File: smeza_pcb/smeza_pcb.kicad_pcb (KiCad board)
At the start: 2 copper layers, 76.2 x 76.2 mm, 59 parts, among them J1 SS-90000-002, J2 SS-90000-002, J3 Conn_01x03, J4 Conn_01x04, J5 Conn_01x03, J6 Conn_01x03, J7 Conn_01x03, J8 Conn_01x03, J9 Conn_02x03_Odd_Even, SW1 SW_DIP_x04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

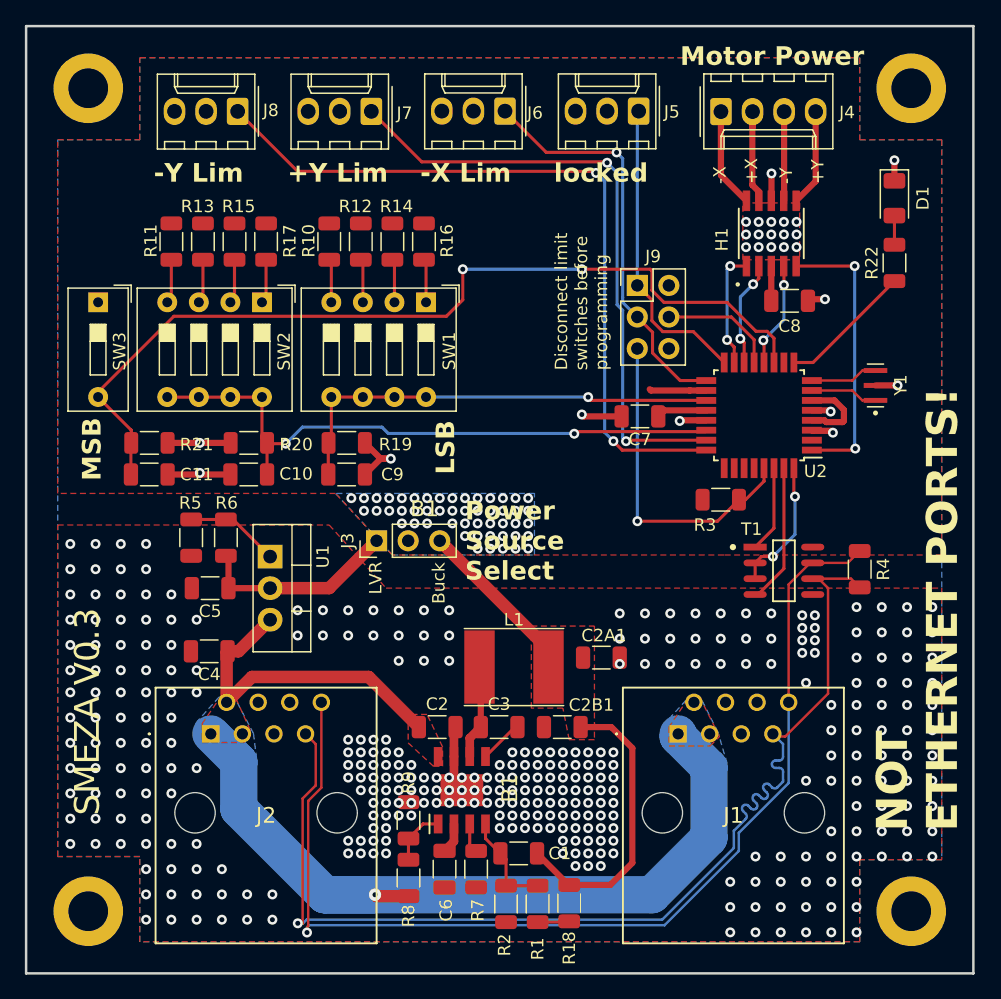
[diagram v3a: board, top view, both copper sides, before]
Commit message: Replaced most extended parts. Swapped out many 1206 resistors for 0805 resistors. Swapped out C1. Swapped out LED. Made all headers DNP. Rerouted to reflect the new footprints.
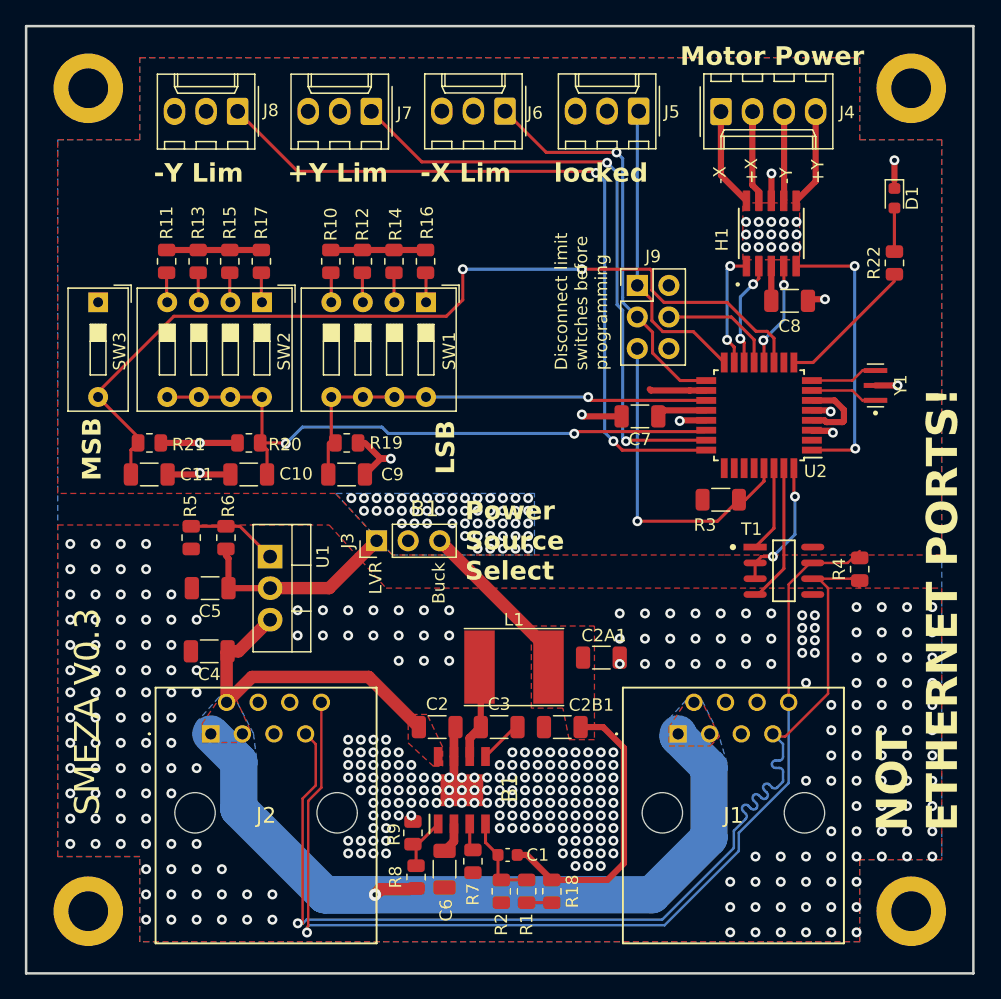
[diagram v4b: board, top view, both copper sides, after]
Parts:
- C1: footprint Capacitor_SMD:C_1206_3216Metric -> Capacitor_SMD:C_0603_1608Metric
- D1: footprint LED_SMD:LED_1206_3216Metric -> LED_SMD:LED_0603_1608Metric
- R1, R10, R11, R12, R13, R14, R15, R16, R17, R18, R19, R2, R20, R21, R22, R4, R5, R6, R7, R8, R9: footprint Resistor_SMD:R_1206_3216Metric -> Resistor_SMD:R_0805_2012Metric
- moved R18 1.69 mm to (143.9, 122.9)
- moved R11 1.63 mm to (112.9, 72.3)
- moved R13 1.63 mm to (115.4, 72.3)
- moved R15 1.63 mm to (118.0, 72.3)
- moved R17 1.63 mm to (120.5, 72.3)
- moved R10 1.59 mm to (126.1, 72.3)
- moved R12 1.59 mm to (128.7, 72.3)
- moved R14 1.59 mm to (131.2, 72.3)
- moved R16 1.59 mm to (133.7, 72.3)
- moved R1 1.35 mm to (141.9, 122.9)
- moved R2 1.09 mm to (139.8, 122.9)
- moved R9 1.07 mm to (132.7, 118.2)
- moved C1 0.90 mm to (140.3, 120.0)
- moved R7 0.69 mm to (137.5, 120.5)
- moved R8 0.61 mm to (133.0, 121.8)
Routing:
- net /+5V: track 13.8 -> 29.1 mm
- net Net-(D1-A): track 2.34 -> 3.50 mm
- net Net-(R15-Pad2): track 3.56 -> 2.40 mm
- net Net-(R13-Pad2): track 3.56 -> 2.40 mm
- net Net-(R11-Pad2): track 3.56 -> 2.40 mm
- net Net-(R17-Pad2): track 3.56 -> 2.40 mm
- net Net-(B1-FB): track 8.19 -> 7.06 mm
- net Net-(R14-Pad2): track 3.49 -> 2.40 mm
- net Net-(R12-Pad2): track 3.49 -> 2.40 mm
- net Net-(R10-Pad2): track 3.49 -> 2.40 mm
- net Net-(R16-Pad2): track 3.49 -> 2.40 mm
- net /DIPS58: track 50.3 -> 50.9 mm
- net /TransceiverDriverEnable: track 11.4 -> 10.8 mm
- net Net-(R1-Pad1): track 2.57 -> 2.03 mm

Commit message: Added tooling holes
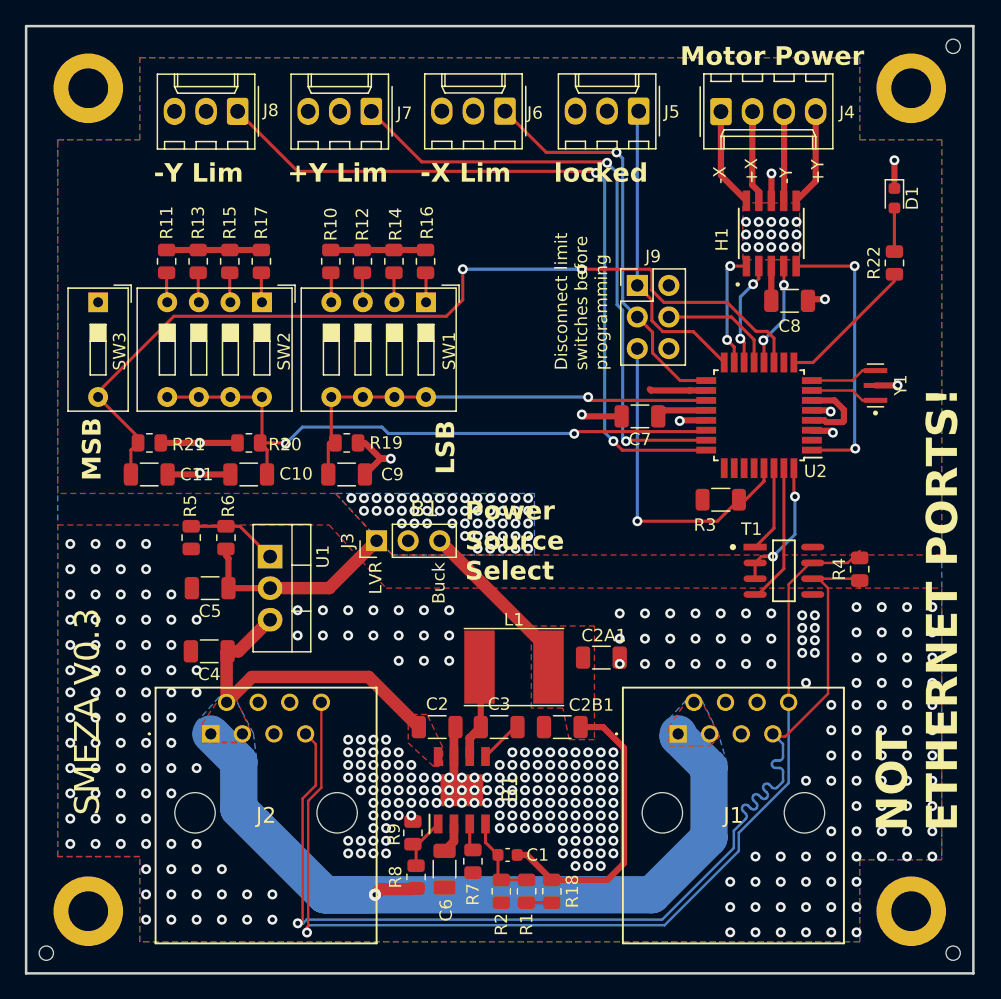
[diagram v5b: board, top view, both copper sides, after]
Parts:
- added FAB**: ToolingHole, Footprints:ToolingHole, F.Cu at (176.2, 55.0)
- added FAB**: ToolingHole, Footprints:ToolingHole, F.Cu at (103.2, 127.9)
- added FAB**: ToolingHole, Footprints:ToolingHole, F.Cu at (176.2, 127.9)
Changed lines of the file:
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@@
     )
+  )
+  (footprint "Footprints:ToolingHole" (layer "F.Cu")
+    (at 176.1744 54.9656)
+    (attr through_hole board_only)
+    (fp_text reference "FAB**" (at 0 -0.5 unlocked) (layer "F.Fab")
+        (effects (font (size 1 1) (thickness 0.1)))
+    )
+    (fp_text value "ToolingHole" (at 0 1 unlocked) (layer "F.Fab")
+        (effects (font (size 1 1) (thickness 0.15)))
+    )
+    (fp_text user "${REFERENCE}" (at 0 2.5 unlocked) (layer "F.Fab")
+        (effects (font (size 1 1) (thickness 0.15)))
+    )
+    (fp_circle (center 0 0) (end 1.016 0)
+      (stroke (width 0.05) (type solid)) (fill none) (layer "B.CrtYd"))
+    (fp_circle (center 0 0) (end 1.016 0)
+      (stroke (width 0.05) (type solid)) (fill none) (layer "F.CrtYd"))
+    (pad "" np_thru_hole circle (at 0 0) (size 1.152 1.152) (drill 1.152) (layers "F&B.Cu" "*.Mask")
+      (solder_mask_margin 0.148))
   )
   (footprint "Resistor_SMD:R_0805_2012Metric" (layer "F.Cu")
@@
     (pad "1" thru_hole circle locked (at 0 0) (size 5.6 5.6) (drill 3.2) (layers "*.Cu" "*.Mask"))
   )
+  (footprint "Footprints:ToolingHole" (layer "F.Cu")
+    (at 103.2256 127.9144)
+    (attr through_hole board_only)
+    (fp_text reference "FAB**" (at 0 -0.5 unlocked) (layer "F.Fab")
+        (effects (font (size 1 1) (thickness 0.1)))
+    )
+    (fp_text value "ToolingHole" (at 0 1 unlocked) (layer "F.Fab")
+        (effects (font (size 1 1) (thickness 0.15)))
+    )
+    (fp_text user "${REFERENCE}" (at 0 2.5 unlocked) (layer "F.Fab")
+        (effects (font (size 1 1) (thickness 0.15)))
+    )
+    (fp_circle (center 0 0) (end 1.016 0)
+      (stroke (width 0.05) (type solid)) (fill none) (layer "B.CrtYd"))
+    (fp_circle (center 0 0) (end 1.016 0)
+      (stroke (width 0.05) (type solid)) (fill none) (layer "F.CrtYd"))
+    (pad "" np_thru_hole circle (at 0 0) (size 1.152 1.152) (drill 1.152) (layers "F&B.Cu" "*.Mask")
+      (solder_mask_margin 0.148))
+  )
+  (footprint "Footprints:ToolingHole" (layer "F.Cu")
+    (at 176.1744 127.9144)
+    (attr through_hole board_only)
+    (fp_text reference "FAB**" (at 0 -0.5 unlocked) (layer "F.Fab")
+        (effects (font (size 1 1) (thickness 0.1)))
+    )
+    (fp_text value "ToolingHole" (at 0 1 unlocked) (layer "F.Fab")
+        (effects (font (size 1 1) (thickness 0.15)))
+    )
+    (fp_text user "${REFERENCE}" (at 0 2.5 unlocked) (layer "F.Fab")
+        (effects (font (size 1 1) (thickness 0.15)))
+    )
+    (fp_circle (center 0 0) (end 1.016 0)
+      (stroke (width 0.05) (type solid)) (fill none) (layer "B.CrtYd"))
+    (fp_circle (center 0 0) (end 1.016 0)
+      (stroke (width 0.05) (type solid)) (fill none) (layer "F.CrtYd"))
+    (pad "" np_thru_hole circle (at 0 0) (size 1.152 1.152) (drill 1.152) (layers "F&B.Cu" "*.Mask")
+      (solder_mask_margin 0.148))
+  )
   (footprint "Capacitor_SMD:C_1206_3216Metric" (layer "F.Cu")

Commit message: Added fiducials and checked component spacing. Removed old JLCPCB files
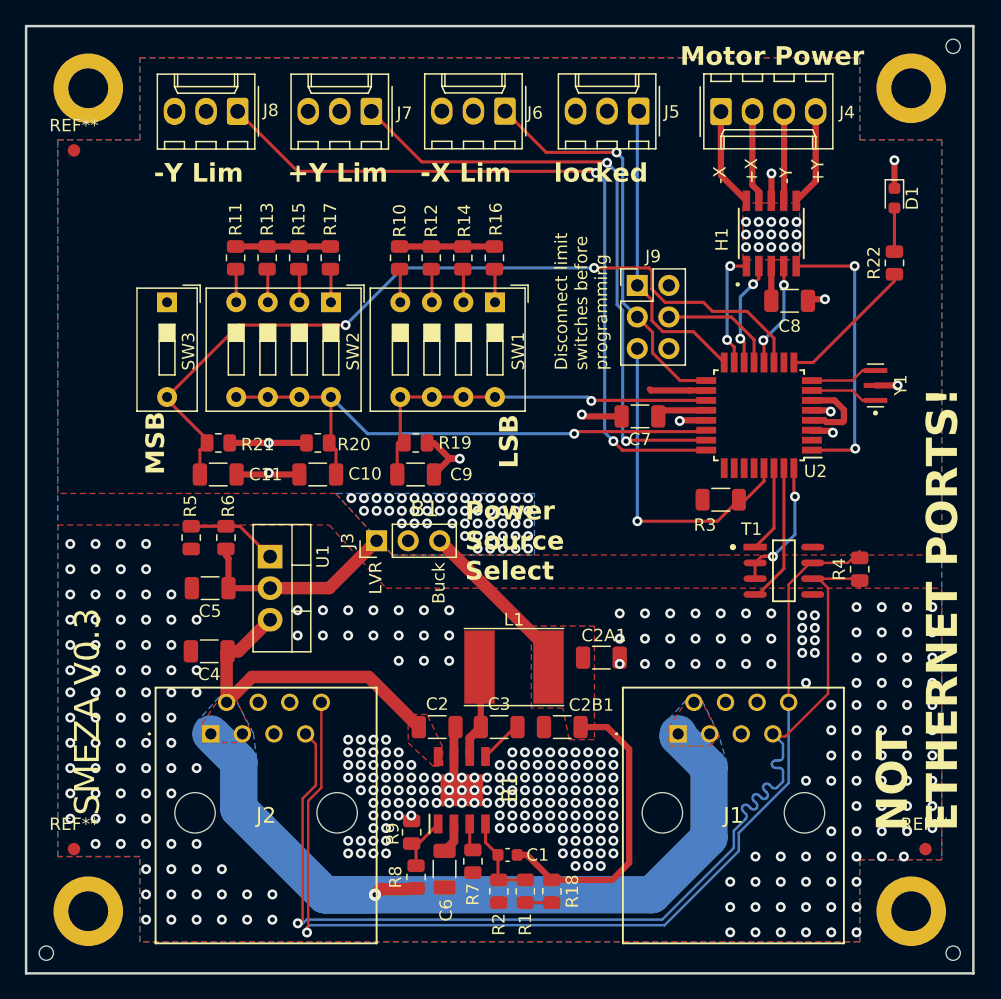
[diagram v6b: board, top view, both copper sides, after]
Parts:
- added REF**: Fiducial_1mm_Mask2mm, Fiducial:Fiducial_1mm_Mask2mm, F.Cu at (105.5, 63.3)
- added REF**: Fiducial_1mm_Mask2mm, Fiducial:Fiducial_1mm_Mask2mm, F.Cu at (173.9, 119.5)
- added REF**: Fiducial_1mm_Mask2mm, Fiducial:Fiducial_1mm_Mask2mm, F.Cu at (105.5, 119.5)
- moved R13 5.56 mm to (121.0, 72.0)
- moved R17 5.56 mm to (126.1, 72.0)
- moved R11 5.56 mm to (118.5, 72.0)
- moved R15 5.56 mm to (123.5, 72.0)
- moved C11 5.55 mm to (117.1, 89.4)
- moved C9 5.55 mm to (132.9, 89.4)
- moved SW3 5.55 mm to (112.9, 75.6)
- moved C10 5.55 mm to (125.1, 89.4)
- moved R19 5.55 mm to (132.9, 86.9)
- moved R20 5.55 mm to (125.1, 86.9)
- moved R21 5.55 mm to (117.1, 86.9)
- moved SW2 5.55 mm to (126.1, 75.6)
- moved SW1 5.55 mm to (139.3, 75.6)
- moved R16 5.54 mm to (139.3, 72.0)
- moved R10 5.54 mm to (131.6, 72.0)
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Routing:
- net /DIP9: track 73.3 -> 66.1 mm
- net /DIPS14: track 36.6 -> 31.1 mm
- net /DIPS58: track 50.9 -> 45.7 mm, vias 2 -> 1
- net /Buck+5V: track 38.3 -> 39.1 mm
- net GND: vias 372 -> 370

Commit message: Fixed part rotations. Fixed silkscreen goofs. Added solder jumpers.
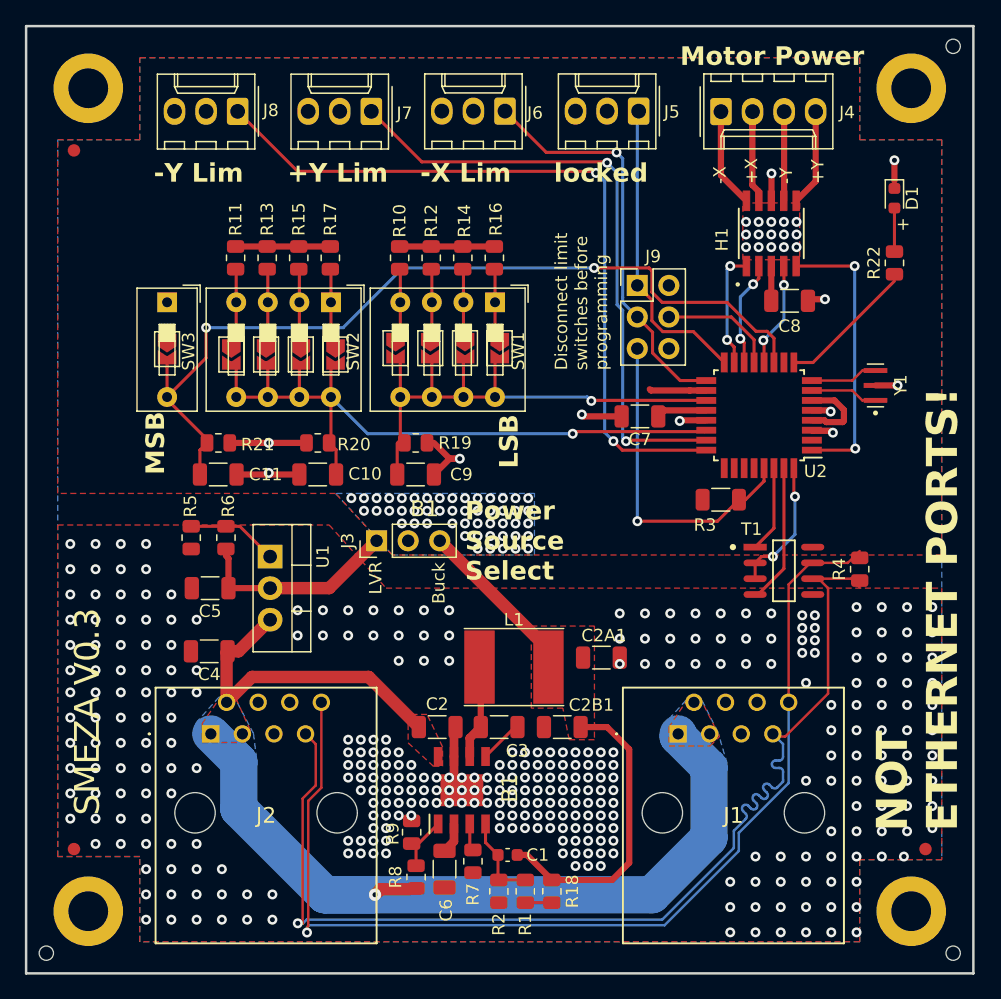
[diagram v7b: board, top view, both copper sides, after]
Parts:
- added JP1: SolderJumper_2_Open, Jumper:SolderJumper-2_P1.3mm_Open_TrianglePad1.0x1.5mm, F.Cu at (139.7, 79.2)
- added JP2: SolderJumper_2_Open, Jumper:SolderJumper-2_P1.3mm_Open_TrianglePad1.0x1.5mm, F.Cu at (136.9, 79.2)
- added JP3: SolderJumper_2_Open, Jumper:SolderJumper-2_P1.3mm_Open_TrianglePad1.0x1.5mm, F.Cu at (134.1, 79.2)
- added JP4: SolderJumper_2_Open, Jumper:SolderJumper-2_P1.3mm_Open_TrianglePad1.0x1.5mm, F.Cu at (131.3, 79.2)
- added JP5: SolderJumper_2_Open, Jumper:SolderJumper-2_P1.3mm_Open_TrianglePad1.0x1.5mm, F.Cu at (118.1, 79.8)
- added JP6: SolderJumper_2_Open, Jumper:SolderJumper-2_P1.3mm_Open_TrianglePad1.0x1.5mm, F.Cu at (120.9, 79.8)
- added JP7: SolderJumper_2_Open, Jumper:SolderJumper-2_P1.3mm_Open_TrianglePad1.0x1.5mm, F.Cu at (123.7, 79.8)
- added JP8: SolderJumper_2_Open, Jumper:SolderJumper-2_P1.3mm_Open_TrianglePad1.0x1.5mm, F.Cu at (126.5, 79.8)
- added JP9: SolderJumper_2_Open, Jumper:SolderJumper-2_P1.3mm_Open_TrianglePad1.0x1.5mm, F.Cu at (112.9, 79.3)
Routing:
- net /DIPS14: track 31.1 -> 44.3 mm
- net /DIPS58: track 45.7 -> 56.9 mm
- net /DIP9: track 66.1 -> 70.8 mm
- net Net-(JP5-A): track 2.68 -> 6.32 mm
- net Net-(JP8-A): track 2.68 -> 6.31 mm
- net Net-(JP6-A): track 2.68 -> 6.22 mm
- net Net-(JP7-A): track 2.68 -> 6.21 mm
- net Net-(JP4-A): track 2.69 -> 5.81 mm
- net Net-(JP1-A): track 2.69 -> 5.81 mm
- net Net-(JP3-A): track 2.69 -> 5.70 mm
- net Net-(JP2-A): track 2.69 -> 5.70 mm
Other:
- board text added: "+"
